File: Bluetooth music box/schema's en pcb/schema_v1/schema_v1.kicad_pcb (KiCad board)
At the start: 4 copper layers, 137.7 x 65.5 mm, 157 parts, among them J1 Conn_01x04, J2 USB_B_Micro, J3 Conn_01x05_Male, SW1 SW_Push, SW2 SW_Push, SW3 SW_Push, SW4 SW_Push, SW5 SW_Push, SW6 SW_Push, SW9 Switch, U1 TL072, U11 tpa3140, U12 LTC4001, U2 SN74LVC1T45DBV, U3 RN52, U4 STM32L443CCTx, U5 FT232RL, U6 LM1117-3.3, U7 TLV61048, U9 Spi_header

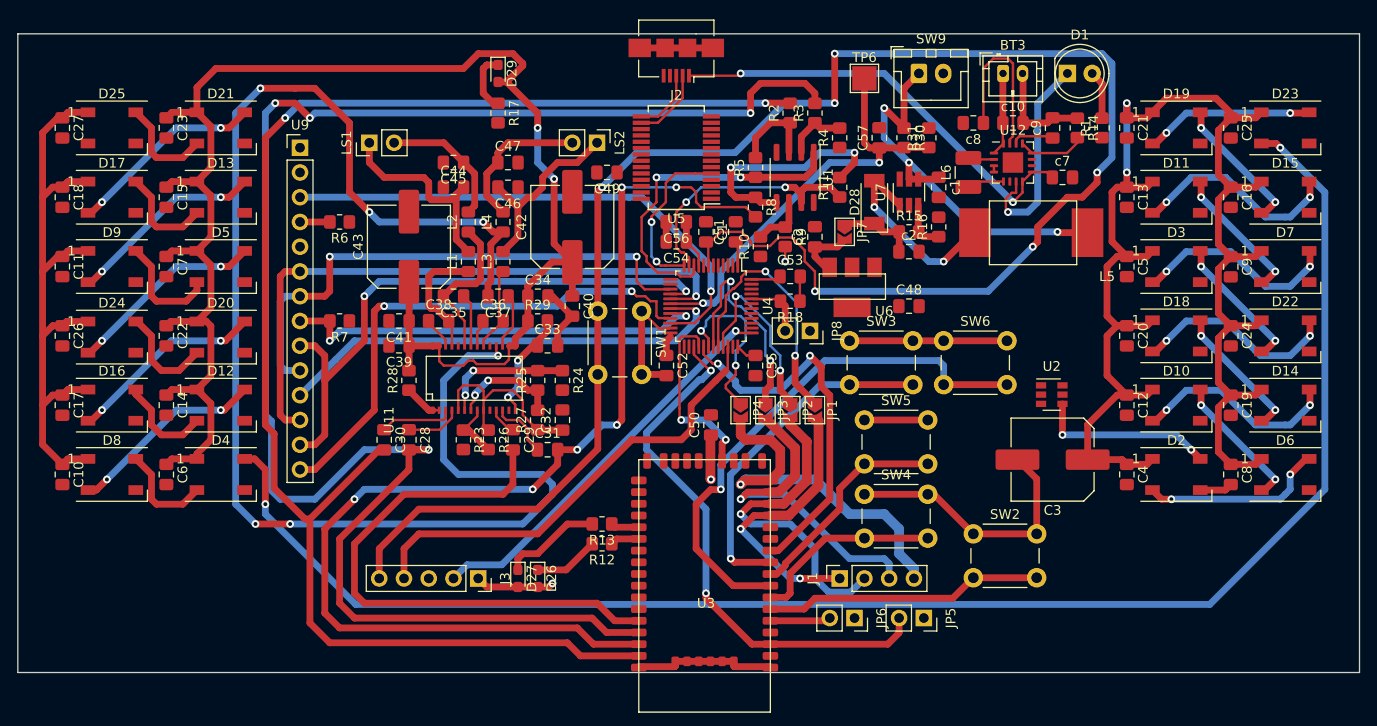
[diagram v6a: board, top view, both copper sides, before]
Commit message: pcb af
laatste tracks verbonden
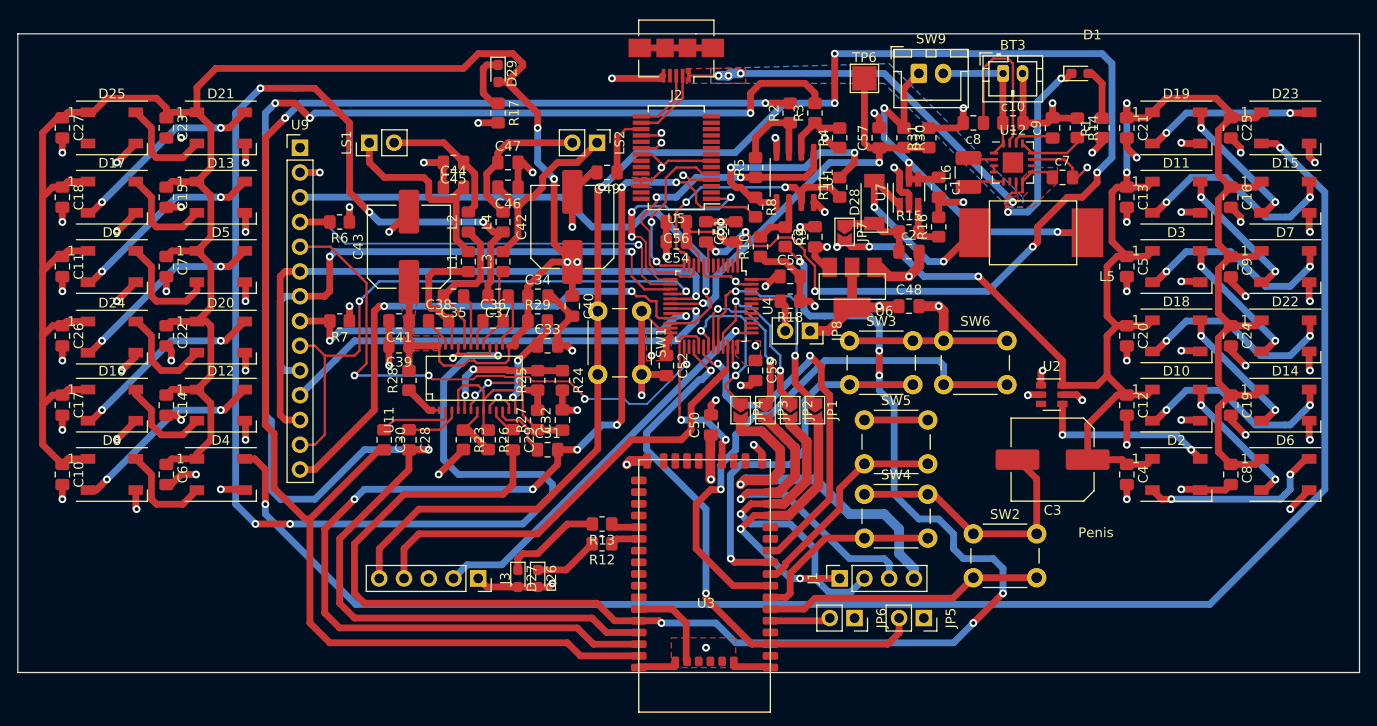
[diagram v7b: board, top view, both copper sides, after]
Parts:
- D1: footprint LED_THT:LED_D5.0mm -> LED_SMD:LED_0603_1608Metric_Pad1.05x0.95mm_HandSolder
- moved D1 1.28 mm to (188.2, 56.9)
- moved C55 0.51 mm to (154.9, 87.4)
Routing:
- net GND: track 104.3 -> 342.3 mm, vias 0 -> 85
- net /R-: track 59.3 -> 149.5 mm, vias 1 -> 6
- net +5V: track 375.5 -> 448.5 mm, vias 4 -> 10
- net LCD_DC: track 0.00 -> 57.6 mm, vias 0 -> 4
- net LCD_rst: track 3.06 -> 45.3 mm, vias 0 -> 1
- net +3V3: track 28.5 -> 65.6 mm, vias 2 -> 15
- net RX: track 0.00 -> 22.9 mm, vias 0 -> 3
- net Net-(C49-Pad1): track 0.00 -> 6.41 mm
- net Net-(BT3-Pad1): track 8.61 -> 14.7 mm
- net TX_BT: track 22.6 -> 17.7 mm
- net vol-: track 35.4 -> 38.4 mm
- net MODE: track 39.1 -> 41.5 mm
- net RTS_BT: track 26.7 -> 24.8 mm
- net Reset: track 184.8 -> 186.3 mm, vias 6 -> 8
- net Vusb: track 45.1 -> 43.6 mm, vias 2 -> 4
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- added copper zone on F.Cu, net +3V3
- added copper zone on In1.Cu, net +3V3
- added copper zone on F.Cu, net +5V
- added copper zone on F.Cu, net GND
- added copper zone on In2.Cu, net GND
- added copper zone on B.Cu, net Vusb
- added copper zone on F.Cu, net Vusb
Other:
- board text added: "Penis"

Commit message: pcb af en gerbers aangemaakt om te bestellen
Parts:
- added .: TestPoint_THTPad_D4.0mm_Drill2.0mm, TestPoint:TestPoint_THTPad_D4.0mm_Drill2.0mm, F.Cu at (213.4, 114.8)
- added .: TestPoint_THTPad_D4.0mm_Drill2.0mm, TestPoint:TestPoint_THTPad_D4.0mm_Drill2.0mm, F.Cu at (213.4, 56.4)
- added .: TestPoint_THTPad_D4.0mm_Drill2.0mm, TestPoint:TestPoint_THTPad_D4.0mm_Drill2.0mm, F.Cu at (82.8, 56.4)
- added .: TestPoint_THTPad_D4.0mm_Drill2.0mm, TestPoint:TestPoint_THTPad_D4.0mm_Drill2.0mm, F.Cu at (82.8, 114.8)
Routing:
- net /STM32G0/LedData: track 0.00 -> 55.5 mm, vias 0 -> 4
- net GND: track 342.3 -> 355.9 mm, vias 85 -> 87
- net DataLeds: track 0.00 -> 3.86 mm
- net +3V3: track 65.6 -> 67.5 mm
- net /L+: track 153.0 -> 153.8 mm
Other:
- board text added: "Robbe Janssens /// PE 2020-2021 /// 2EH1"
- board text removed: "Penis"
